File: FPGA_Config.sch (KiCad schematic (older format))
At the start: 2 parts, among them J1 104031-0811, U1 XA7Z020-1CLG400Q

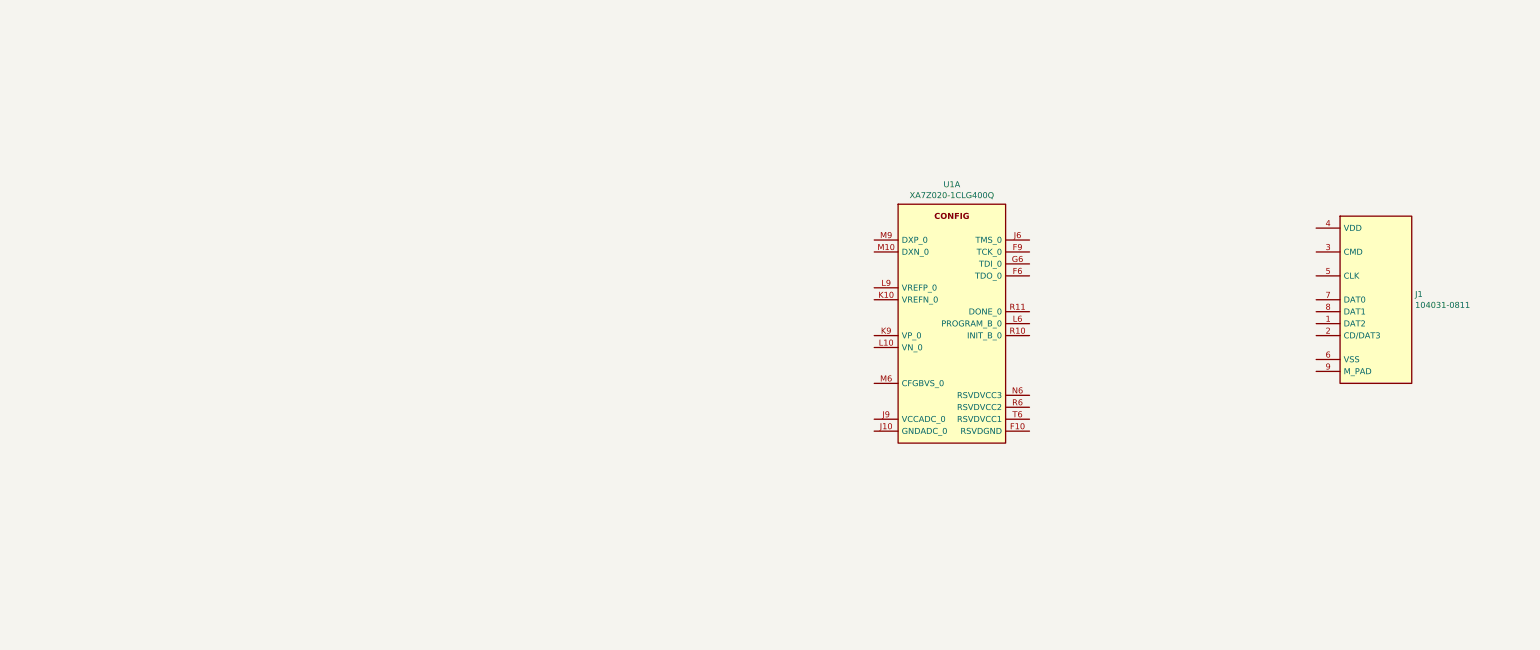
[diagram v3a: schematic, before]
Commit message: Completed FPGA power sheet completed USB3 completed FPGA config
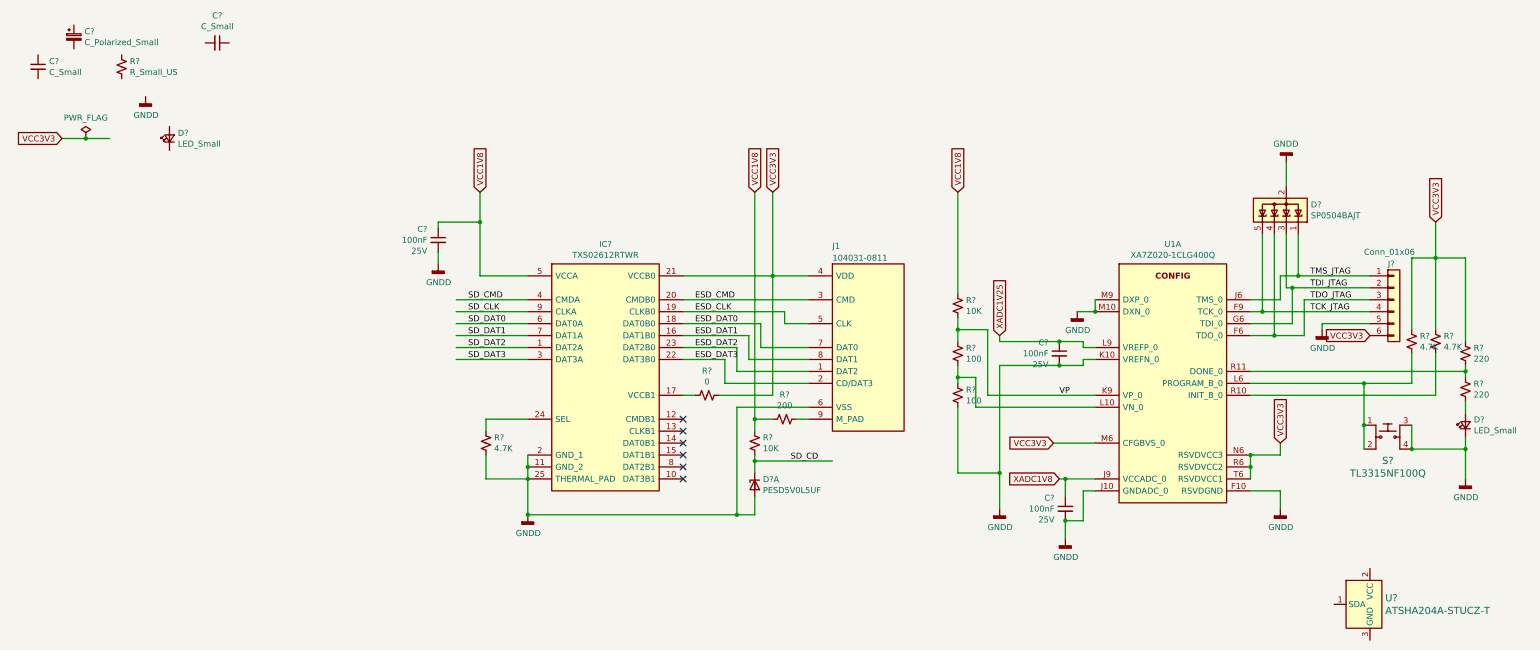
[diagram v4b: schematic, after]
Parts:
- added C?: C_Small, Capacitor_SMD:C_0603_1608Metric_Pad1.08x0.95mm_HandSolder, symbol Device:C_Small
- added C?: C_Polarized_Small, Capacitor_Tantalum_SMD:CP_EIA-1608-10_AVX-L_Pad1.25x1.05mm_HandSolder, symbol Device:C_Polarized_Small
- added C?: C_Small, symbol Device:C_Small
- added C? (x3): 100nF, Capacitor_SMD:C_0603_1608Metric_Pad1.08x0.95mm_HandSolder, symbol Device:C_Small
- added D?: PESD5V0L5UF, Package_TO_SOT_SMD:SOT-886, symbol Power_Protection:PESD5V0L5UF
- added D? (x2): LED_Small, symbol Device:LED_Small
- added D?: SP0504BAJT, Package_TO_SOT_SMD:SOT-353_SC-70-5, symbol Power_Protection:SP0504BAJT
- added IC?: TXS02612RTWR, QFN50P400X400X80-25N-D, symbol GM_Level_Shifters:TXS02612RTWR
- added J?: Conn_01x06, symbol Connector_Generic:Conn_01x06
- added R?: R_Small_US, Resistor_SMD:R_0603_1608Metric_Pad0.98x0.95mm_HandSolder, symbol Device:R_Small_US
- added R?: 0, Resistor_SMD:R_0603_1608Metric_Pad0.98x0.95mm_HandSolder, symbol Device:R_Small_US
- added R? (x2): 10K, Resistor_SMD:R_0603_1608Metric_Pad0.98x0.95mm_HandSolder, symbol Device:R_Small_US
- added R?: 200, Resistor_SMD:R_0603_1608Metric_Pad0.98x0.95mm_HandSolder, symbol Device:R_Small_US
- added R? (x3): 4.7K, Resistor_SMD:R_0603_1608Metric_Pad0.98x0.95mm_HandSolder, symbol Device:R_Small_US
- added R? (x2): 220, Resistor_SMD:R_0603_1608Metric_Pad0.98x0.95mm_HandSolder, symbol Device:R_Small_US
- added R? (x2): 100, Resistor_SMD:R_0603_1608Metric_Pad0.98x0.95mm_HandSolder, symbol Device:R_Small_US
- added S?: TL3315NF100Q, digikey-footprints:Switch_Tactile_SMD_4.5x4.5mm_TL3315NF160Q, symbol dk_Tactile-Switches:TL3315NF160Q
- added U?: ATSHA204A-STUCZ-T, digikey-footprints:SOT-23-3, symbol dk_Specialized-ICs:ATSHA204A-STUCZ-T
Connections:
- net labels added: ESD_CLK, ESD_CMD, ESD_DAT0, ESD_DAT1, ESD_DAT2, ESD_DAT3, GNDD, SD_CD, SD_CLK, SD_CMD, SD_DAT0, SD_DAT1, SD_DAT2, SD_DAT3, TCK_JTAG, TDI_JTAG, TDO_JTAG, TMS_JTAG, VCC1V8, VCC3V3, VP, XADC1V25, XADC1V8
- wire segments 0 -> 137
- no-connect marks 0 -> 6
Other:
- moved on the sheet: J1, U1A

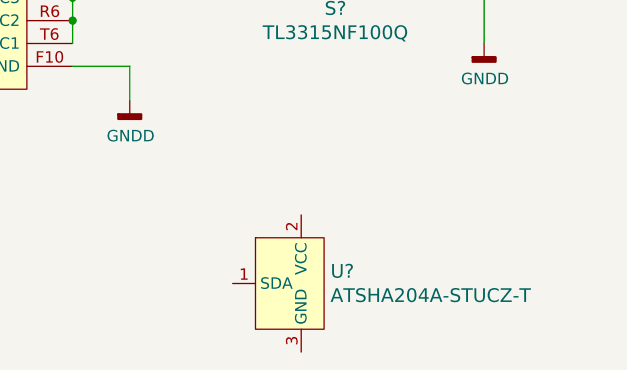
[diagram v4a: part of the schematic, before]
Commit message: Added sheet Ext_Analog
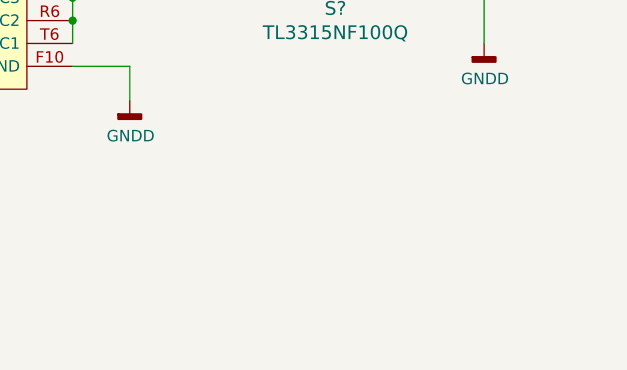
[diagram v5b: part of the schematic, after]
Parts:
- removed U?: ATSHA204A-STUCZ-T, digikey-footprints:SOT-23-3, symbol dk_Specialized-ICs:ATSHA204A-STUCZ-T
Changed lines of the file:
@@
 Text GLabel 9350 3300 0    50   Input ~ 0
 VCC3V3
-$Comp
-L dk_Specialized-ICs:ATSHA204A-STUCZ-T U?
-U 1 1 60664A56
-P 9350 5550
-F 0 "U?" H 9478 5603 60  0000 L CNN
-F 1 "ATSHA204A-STUCZ-T" H 9478 5497 60  0000 L CNN
-F 2 "digikey-footprints:SOT-23-3" H 9550 5750 60  0001 L CNN
-F 3 "http://www.microchip.com/mymicrochip/filehandler.aspx?ddocname=en590027" H 9550 5850 60  0001 L CNN
-F 4 "ATSHA204A-STUCZ-TCT-ND" H 9550 5950 60  0001 L CNN "Digi-Key_PN"
-F 5 "ATSHA204A-STUCZ-T" H 9550 6050 60  0001 L CNN "MPN"
-F 6 "Integrated Circuits (ICs)" H 9550 6150 60  0001 L CNN "Category"
-F 7 "Specialized ICs" H 9550 6250 60  0001 L CNN "Family"
-F 8 "http://www.microchip.com/mymicrochip/filehandler.aspx?ddocname=en590027" H 9550 6350 60  0001 L CNN "DK_Datasheet_Link"
-F 9 "/product-detail/en/microchip-technology/ATSHA204A-STUCZ-T/ATSHA204A-STUCZ-TCT-ND/4814557" H 9550 6450 60  0001 L CNN "DK_Detail_Page"
-F 10 "IC AUTHENTICATION CHIP SOT23-3" H 9550 6550 60  0001 L CNN "Description"
-F 11 "Microchip Technology" H 9550 6650 60  0001 L CNN "Manufacturer"
-F 12 "Active" H 9550 6750 60  0001 L CNN "Status"
-	1    9350 5550
-	1    0    0    -1
-$EndComp
 $EndSCHEMATC
